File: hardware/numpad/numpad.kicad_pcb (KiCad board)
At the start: 2 copper layers, 83 x 124 mm, 116 parts, among them J1 USB_C_Receptacle_USB2.0_16P, J2 Conn_01x03, J3 Conn_01x04, Q1 BSS138, Q2 BSS138, SW1 BOOTSEL, SW2 RESET, SW3 RotaryEncoder_Switch, U1 NCP1117-3.3_SOT223, U2 USBLC6-2SC6, U3 RP2040, U4 W25Q128JVS, U5 74AHCT1G125, Y1 12MHz

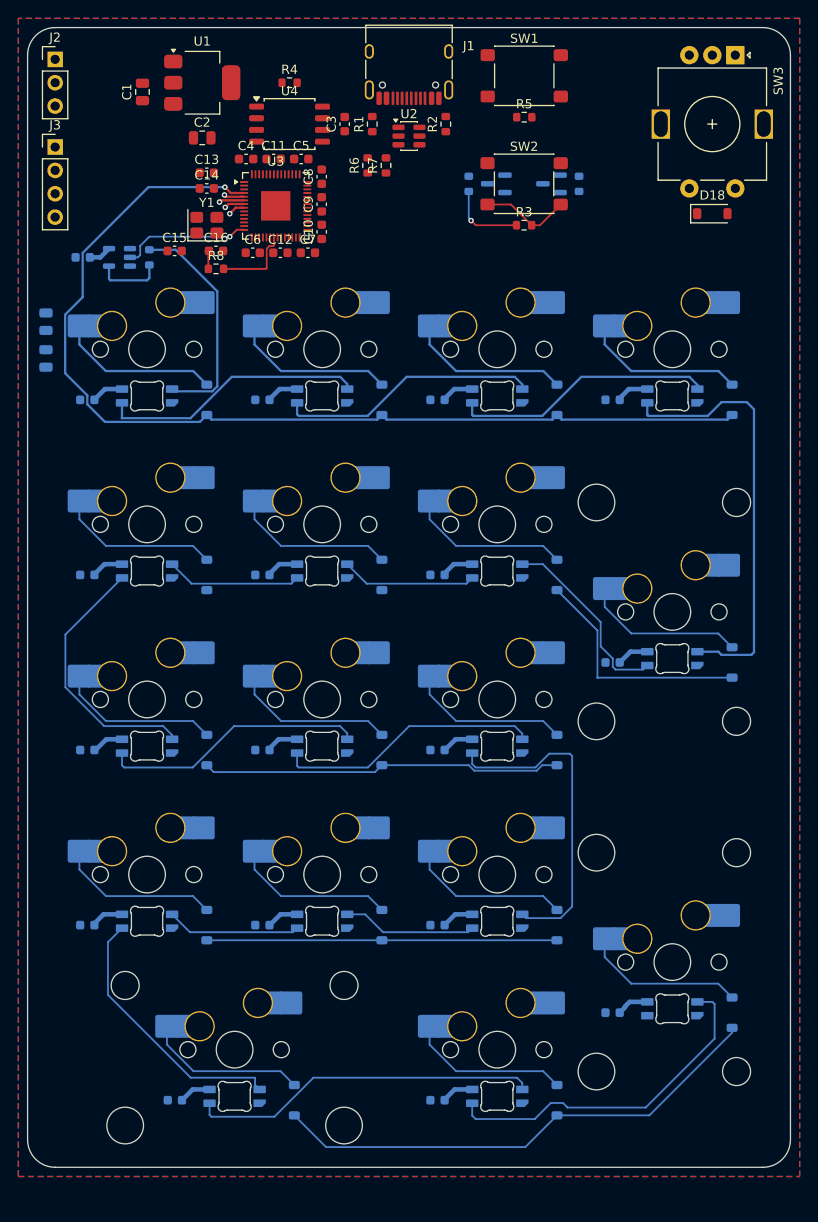
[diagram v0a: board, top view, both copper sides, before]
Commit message: led/sw matrix routing done
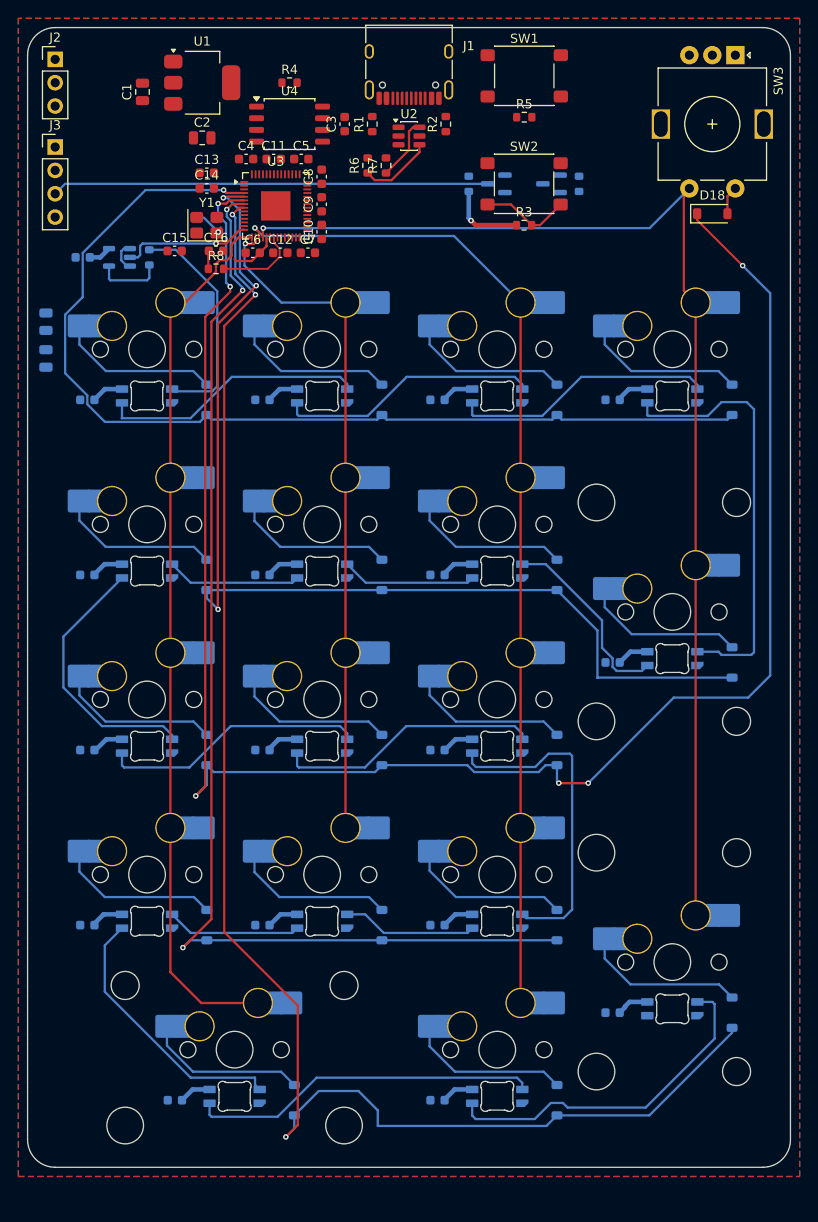
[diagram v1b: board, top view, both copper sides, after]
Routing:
- net /02_mcu/ROW2: track 42.0 -> 196.1 mm, vias 1 -> 6
- net /02_mcu/COL3: track 0.00 -> 129.1 mm, vias 0 -> 1
- net /02_mcu/ROW4: track 56.6 -> 167.0 mm, vias 1 -> 3
- net /02_mcu/COL2: track 0.00 -> 109.7 mm, vias 0 -> 1
- net /02_mcu/COL0: track 0.00 -> 96.8 mm
- net /02_mcu/ROW1: track 28.3 -> 117.5 mm, vias 1 -> 3
- net /02_mcu/ROW3: track 40.3 -> 126.9 mm, vias 1 -> 3
- net /02_mcu/COL1: track 0.00 -> 74.0 mm, vias 0 -> 1
- net Net-(J3-Pin_3): track 0.00 -> 47.5 mm
- net GND: track 0.00 -> 12.2 mm, vias 0 -> 1
- net /01_power_usb/USB_DM: track 0.00 -> 8.03 mm
- net /01_power_usb/USB_DP: track 0.00 -> 6.88 mm
- net Net-(D18-A): track 0.00 -> 3.10 mm

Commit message: full layout-first 0 error DRC
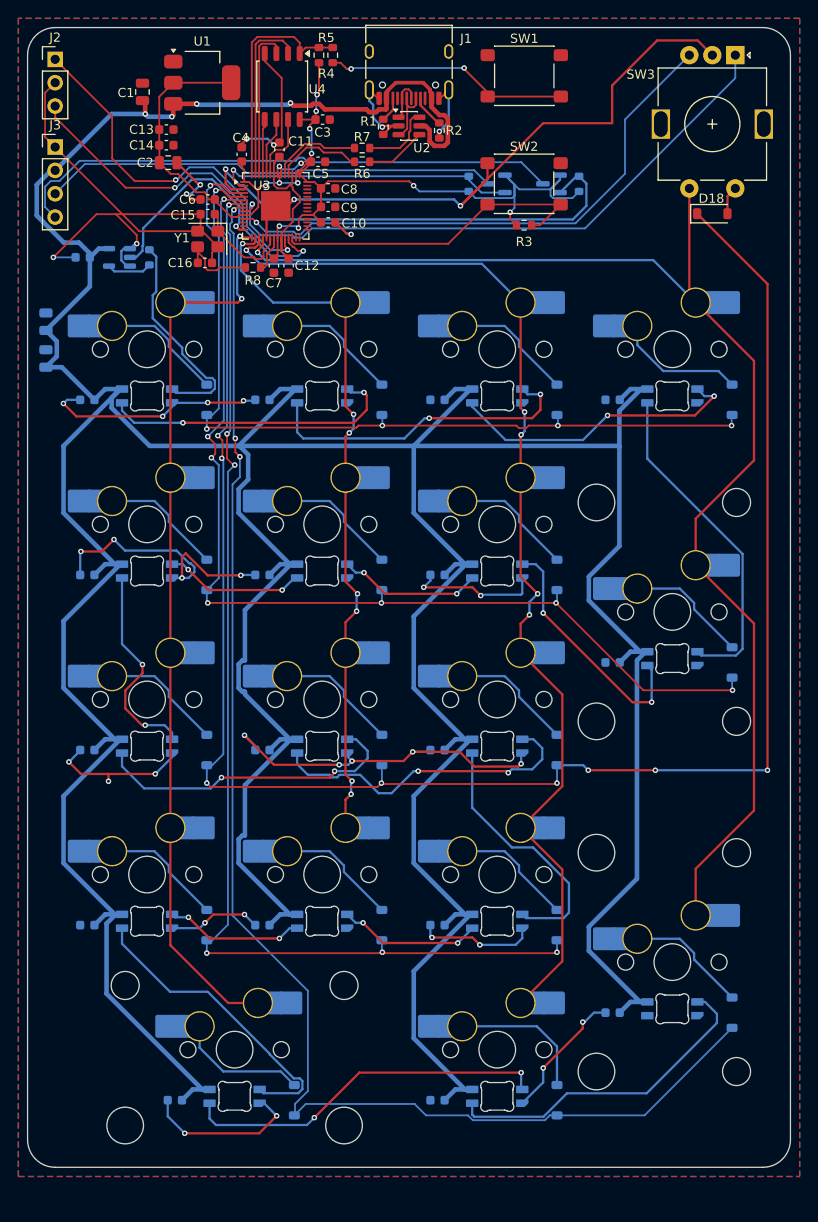
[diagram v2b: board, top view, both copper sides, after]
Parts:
- moved R5 21.9 mm to (80.2, 8.00), turned to 90 degrees
- moved C6 7.59 mm to (66.6, 23.7), turned to 180 degrees
- moved C13 6.44 mm to (62.1, 16.1)
- moved C14 6.44 mm to (62.1, 17.8)
- moved C15 5.38 mm to (66.6, 25.3), turned to 180 degrees
- moved C2 4.58 mm to (62.3, 19.7)
- moved R4 4.39 mm to (78.7, 8.00), turned to 90 degrees
- moved U4 4.16 mm to (74.7, 11.4), turned to -90 degrees
- moved R8 4.03 mm to (71.5, 31.1)
- moved C7 3.96 mm to (73.8, 30.9), turned to -90 degrees
- moved R7 3.22 mm to (83.4, 18.1), turned to 180 degrees
- moved C3 2.44 mm to (79.1, 15.0), turned to 0 degrees
- moved C5 1.85 mm to (78.6, 19.6)
- moved C16 1.77 mm to (66.3, 30.6)
- moved C12 1.66 mm to (75.4, 30.9), turned to -90 degrees
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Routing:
- net +5V: track 62.5 -> 573.2 mm, vias 0 -> 4
- net GND: track 12.2 -> 353.7 mm, vias 1 -> 37
- net +3V3: track 8.43 -> 126.3 mm, vias 1 -> 13
- net /02_mcu/ENC_A: track 0.00 -> 66.9 mm, vias 0 -> 1
- net /02_mcu/ENC_B: track 0.00 -> 60.6 mm, vias 0 -> 1
- net Net-(J3-Pin_4): track 0.00 -> 60.4 mm
- net /02_mcu/I2C_SCL: track 0.00 -> 52.4 mm, vias 0 -> 1
- net /02_mcu/SWCLK: track 0.00 -> 41.0 mm, vias 0 -> 2
- net /02_mcu/SWDIO: track 0.00 -> 40.0 mm, vias 0 -> 2
- net /02_mcu/I2C_SDA: track 0.00 -> 33.3 mm, vias 0 -> 1
- net Net-(R5-Pad1): track 0.00 -> 26.7 mm, vias 0 -> 2
- net Net-(U3-RUN): track 9.82 -> 35.9 mm
- net Net-(U3-~{QSPI_SS}): track 0.00 -> 25.1 mm
- net /02_mcu/DVDD_1V1: track 0.00 -> 19.1 mm
- net Net-(U3-QSPI_SD1): track 0.00 -> 18.9 mm
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
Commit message: throughholes added/bottom board extended, c3/c5/c11 schem value fixed
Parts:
- added REF**: MountingHole_2.2mm_M2, MountingHole:MountingHole_2.2mm_M2, F.Cu at (50.0, 129.0)
- added REF**: MountingHole_2.2mm_M2, MountingHole:MountingHole_2.2mm_M2, F.Cu at (55.8, 8.75)
- added REF**: MountingHole_2.2mm_M2, MountingHole:MountingHole_2.2mm_M2, F.Cu at (114.1, 26.7)
- added REF**: MountingHole_2.2mm_M2, MountingHole:MountingHole_2.2mm_M2, F.Cu at (127.0, 129.0)
- C11, C3, C5: value 100n -> 1u
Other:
- board size 83 x 124 mm -> 83 x 127 mm
